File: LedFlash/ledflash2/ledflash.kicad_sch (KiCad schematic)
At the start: 13 parts, among them J1 Conn_01x02_Pin, SW1 SW_Push, U1 SN74LVC1G14DBV, U2 74HC590A

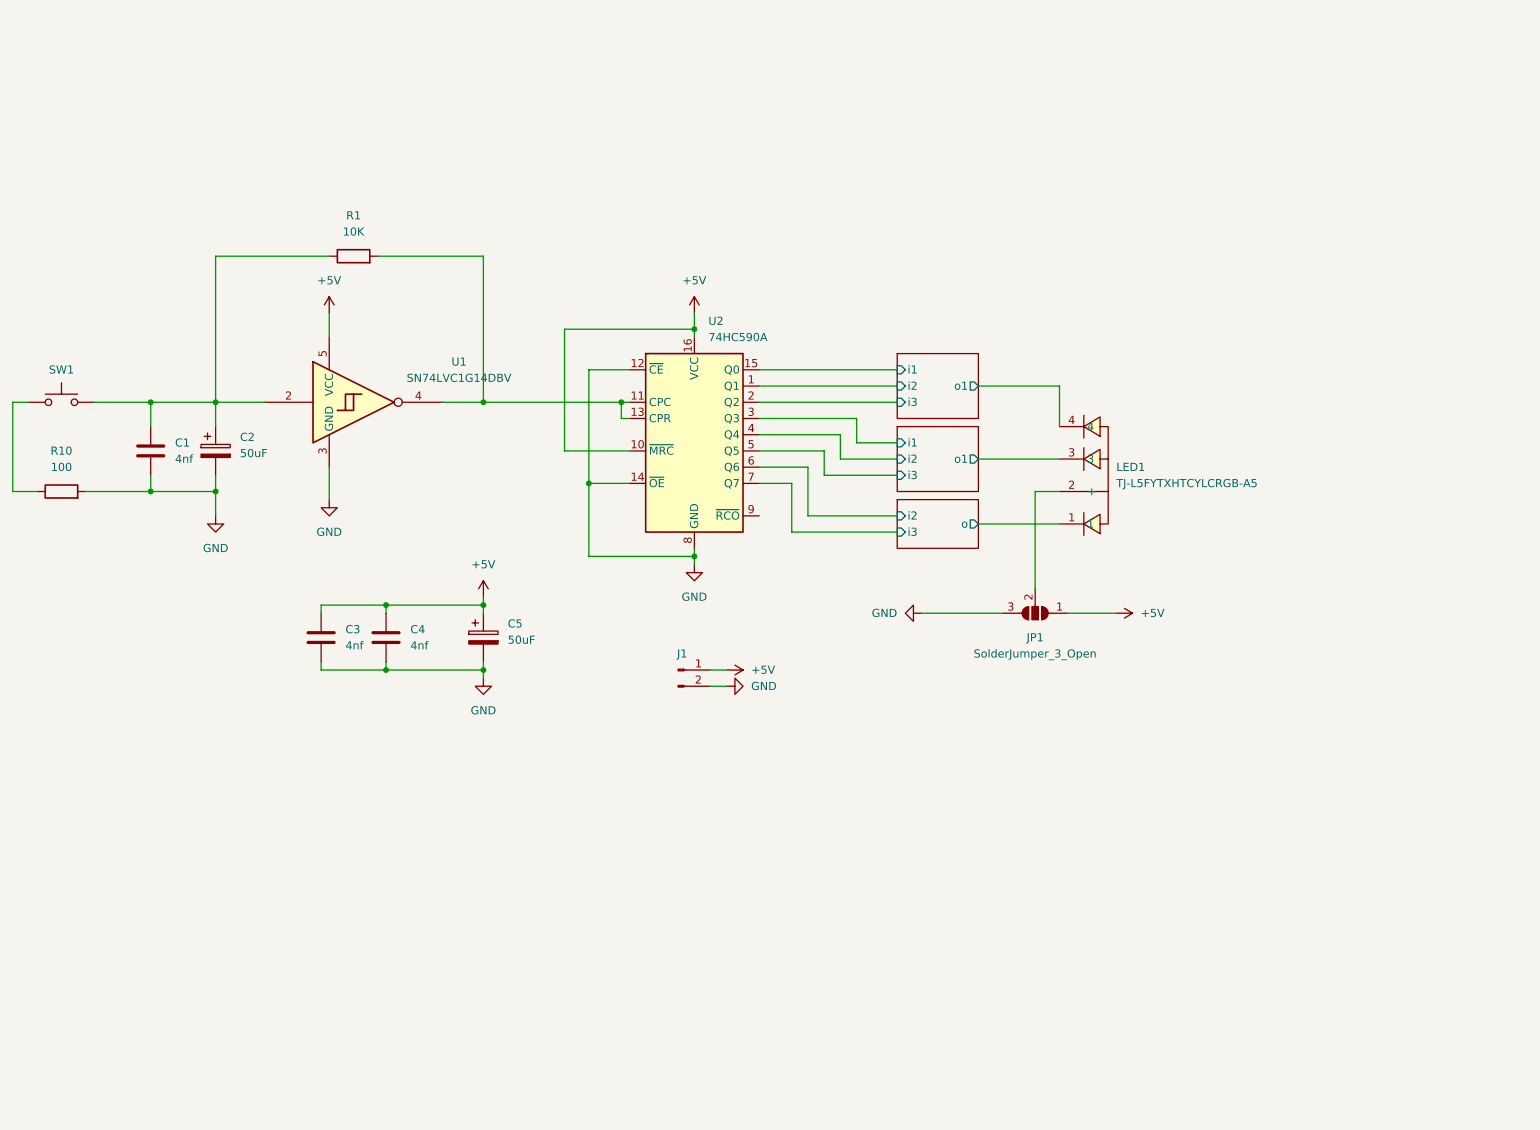
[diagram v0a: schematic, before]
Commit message: Update LED Flash - Added R values, tables and BOM file
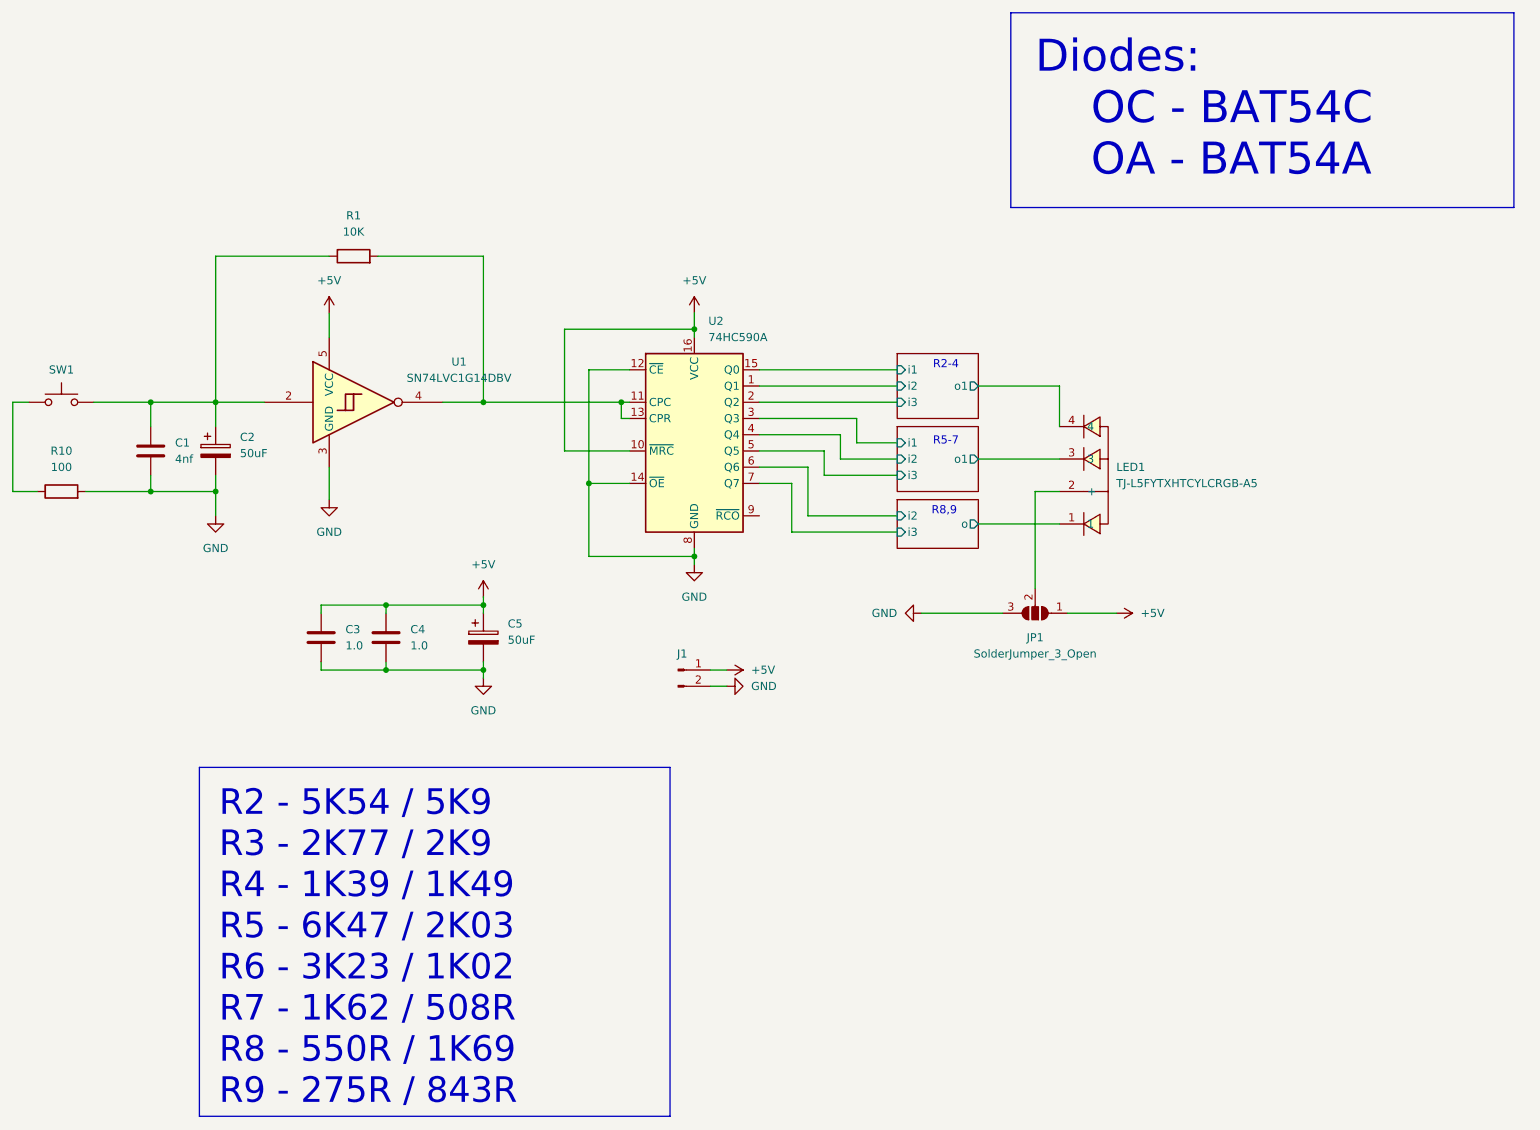
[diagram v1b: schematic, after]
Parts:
- C3, C4: value 4nf -> 1.0
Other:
- note added: "R2-4"
- note added: "R5-7"
- note added: "R8,9"
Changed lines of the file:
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@@
+		)
+	)
+	(text_box "Diodes:\n	OC - BAT54C\n	OA - BAT54A\n"
+		(exclude_from_sim no)
+		(at 200.66 19.05 0)
+		(size 78.74 30.48)
+		(stroke
+			(width 0)
+			(type default)
+		)
+		(fill
+			(type none)
+		)
+		(effects
+			(font
+				(size 5 5)
+			)
+			(justify left top)
+		)
+	)
+	(text_box "R2 - 5K54 / 5K9\nR3 - 2K77 / 2K9\nR4 - 1K39 / 1K49\nR5 - 6K47 / 2K03\nR6 - 3K23 / 1K02\nR7 - 1K62 / 508R\nR8 - 550R / 1K69\nR9 - 275R / 843R"
+		(exclude_from_sim no)
+		(at 73.66 137.16 0)
+		(size 73.66 54.61)
+		(stroke
+			(width 0)
+			(type default)
+		)
+		(fill
+			(type none)
+		)
+		(effects
+			(font
+				(size 4 4)
+			)
+			(justify left top)
+		)
+	)
+	(text "R2-4"
+		(exclude_from_sim no)
+		(at 190.5 74.93 0)
+		(effects
+			(font
+				(size 1.27 1.27)
+			)
+			(justify bottom)
+		)
+	)
+	(text "R5-7"
+		(exclude_from_sim no)
+		(at 190.5 86.868 0)
+		(effects
+			(font
+				(size 1.27 1.27)
+			)
+			(justify bottom)
+		)
+	)
+	(text "R8,9"
+		(exclude_from_sim no)
+		(at 190.246 97.79 0)
+		(effects
+			(font
+				(size 1.27 1.27)
+			)
+			(justify bottom)
 		)
 	)
@@
 			)
 		)
-		(property "Value" "4nf"
+		(property "Value" "1.0"
 			(at 106.68 118.1099 0)
 			(effects
@@
 			)
 		)
-		(property "Value" "4nf"
+		(property "Value" "1.0"
 			(at 96.52 118.1099 0)
 			(effects
@@
 			)
 		)
+		(property "R2" "6K2"
+			(at 182.88 83.82 0)
+			(effects
+				(font
+					(size 1.27 1.27)
+				)
+				(hide yes)
+			)
+		)
+		(property "R3" "3K3"
+			(at 182.88 83.82 0)
+			(effects
+				(font
+					(size 1.27 1.27)
+				)
+				(hide yes)
+			)
+		)
+		(property "R4" "1K6"
+			(at 182.88 83.82 0)
+			(effects
+				(font
+					(size 1.27 1.27)
+				)
+				(hide yes)
+			)
+		)
 		(pin "o1" output
 			(at 195.58 88.9 0)
@@
 				(hide yes)
 			)
+		)
+		(property "R2" "5K6"
+			(at 182.88 72.39 0)
+			(effects
+				(font
+					(size 1.27 1.27)
+				)
+				(hide yes)
+			)
+		)
+		(property "R3" "2K7"
+			(at 182.88 72.39 0)
+			(effects
+				(font
+					(size 1.27 1.27)
+				)
+				(hide yes)
+			)
+		)
+		(property "R4" "1K3"
+			(at 182.88 72.39 0)
+			(effects
+				(font
+					(size 1.27 1.27)
+				)
+				(hide yes)
+			)

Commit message: Start Tetris debugging
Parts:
- C2, C5: now not fitted
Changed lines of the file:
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@@
 		(in_bom yes)
 		(on_board yes)
-		(dnp no)
+		(dnp yes)
 		(fields_autoplaced yes)
 		(property "Reference" "C2"
@@
 					(size 1.27 1.27)
 				)
+				(hide yes)
 			)
 		)
@@
 		(in_bom yes)
 		(on_board yes)
-		(dnp no)
+		(dnp yes)
 		(fields_autoplaced yes)
 		(property "Reference" "C5"
